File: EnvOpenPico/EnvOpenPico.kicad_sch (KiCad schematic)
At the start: 55 parts, among them J2 Button, J3 2.54mm header 01x20, J4 2.54mm header 01x20, J5 Conn_01x03_Male, Q1 SI2301B, U1 SOT-23-5 5.5V 3.3V 500mA, U3 RP2040, Y1 3225_4P 12MHz

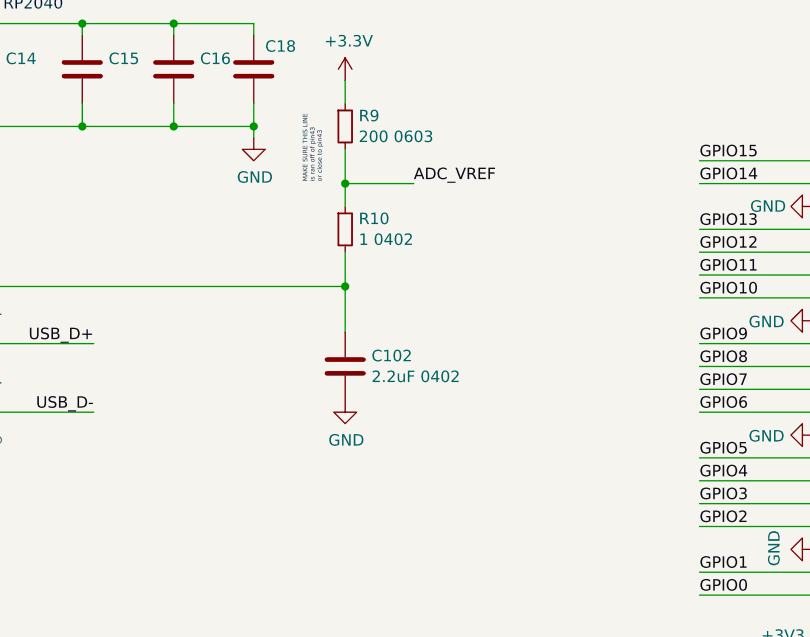
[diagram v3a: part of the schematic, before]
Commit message: re-aligned some parts to be properly centered, not important but wanted to do it.
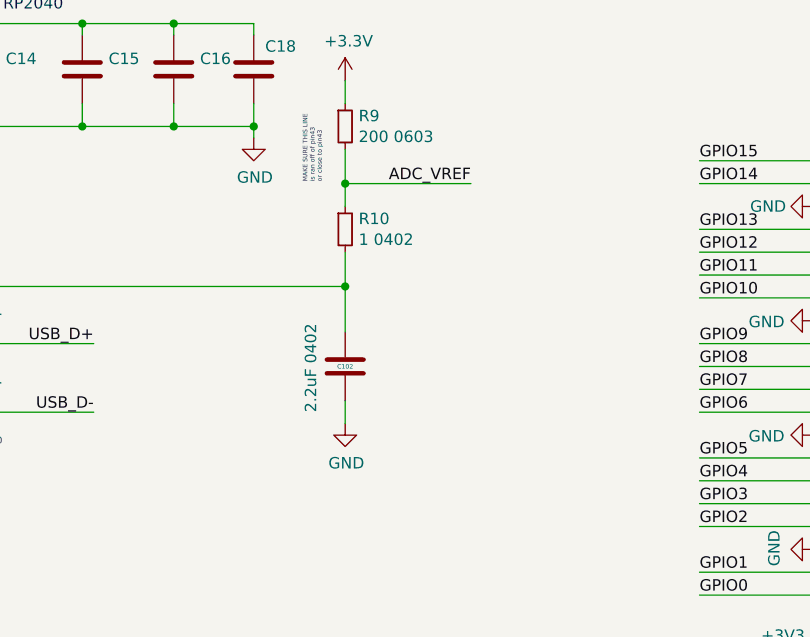
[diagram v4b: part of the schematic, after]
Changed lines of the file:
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@@
     (stroke (width 0) (type default))
   )
+  (wire (pts (xy 290.83 78.74) (xy 304.8 78.74))
+    (stroke (width 0) (type default))
+  )
   (wire (pts (xy 356.87 137.16) (xy 369.57 137.16))
     (stroke (width 0) (type default))
@@
     (stroke (width 0) (type default))
   )
+  (wire (pts (xy 290.83 102.87) (xy 290.83 105.41))
+    (stroke (width 0) (type default))
+  )
   (wire (pts (xy 356.87 101.6) (xy 369.57 101.6))
     (stroke (width 0) (type default))
@@
     (stroke (width 0) (type default))
   )
-  (wire (pts (xy 290.83 78.74) (xy 298.45 78.74))
-    (stroke (width 0) (type default))
-  )
   (wire (pts (xy 369.57 121.92) (xy 356.87 121.92))
     (stroke (width 0) (type default))
@@
     (effects (font (size 1.27 1.27)) (justify left bottom))
   )
-  (label "ADC_VREF" (at 298.45 78.74 0) (fields_autoplaced)
-    (effects (font (size 1.27 1.27)) (justify left bottom))
+  (label "ADC_VREF" (at 304.8 78.74 180) (fields_autoplaced)
+    (effects (font (size 1.27 1.27)) (justify right bottom))
   )
   (label "GPIO2" (at 245.11 116.84 180) (fields_autoplaced)
@@
     )
   )
-  (symbol (lib_id "power:GND") (at 290.83 102.87 0) (unit 1)
+  (symbol (lib_id "power:GND") (at 290.83 105.41 0) (unit 1)
     (in_bom yes) (on_board yes) (dnp no)
-    (property "Reference" "#PWR0101" (at 290.83 109.22 0)
+    (property "Reference" "#PWR0101" (at 290.83 111.76 0)
       (effects (font (size 1.27 1.27)) hide)
     )
-    (property "Value" "GND" (at 290.957 107.2642 0)
+    (property "Value" "GND" (at 290.957 109.8042 0)
       (effects (font (size 1.27 1.27)))
     )
-    (property "Footprint" "" (at 290.83 102.87 0)
+    (property "Footprint" "" (at 290.83 105.41 0)
       (effects (font (size 1.27 1.27)) hide)
     )
-    (property "Datasheet" "" (at 290.83 102.87 0)
+    (property "Datasheet" "" (at 290.83 105.41 0)
       (effects (font (size 1.27 1.27)) hide)
     )
@@
   (symbol (lib_id "Device:C") (at 290.83 99.06 0) (unit 1)
     (in_bom yes) (on_board yes) (dnp no)
-    (property "Reference" "C102" (at 293.751 97.8916 0)
-      (effects (font (size 1.27 1.27)) (justify left))
+    (property "Reference" "C102" (at 290.83 99.06 0)
+      (effects (font (size 0.5 0.5)))
     )
-    (property "Value" "2.2uF 0402" (at 293.751 100.203 0)
+    (property "Value" "2.2uF 0402" (at 287.02 104.14 90)
       (effects (font (size 1.27 1.27)) (justify left))
     )

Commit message: swapped the symbol and footprint for the type-c port to the kicad built in one
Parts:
- removed USB1: TYPE-C-31-M-12, HRO-TYPE-C31-M-12:HRO-TYPE-C-31-M-12, symbol Type-C:HRO-TYPE-C-31-M-12
- added J1: USB_C_Receptacle_USB2.0, Connector_USB:USB_C_Receptacle_HRO_TYPE-C-31-M-12, symbol Connector:USB_C_Receptacle_USB2.0
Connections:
- net GND: now also J1.A1 (GND), J1.A12 (GND), J1.B1 (GND), J1.B12 (GND)
- net USB_D+: now also J1.A6 (D+), J1.B6 (D+)
- net USB_D-: now also J1.A7 (D-), J1.B7 (D-)
- net VBUS: now also J1.A4 (VBUS), J1.A9 (VBUS), J1.B4 (VBUS), J1.B9 (VBUS)
- net at R6.2: now also J1.B5 (CC2)
- net at C101.2, R102.1: now also J1.S1 (SHIELD)
- net at R5.2: now also J1.A5 (CC1)
- no-connect marks 2 -> 0
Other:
- moved on the sheet: C1, C101, C4, C6, C7, CBP1, D1, F1, FB1, NT1, R101, R102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
